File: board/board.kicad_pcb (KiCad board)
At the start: 2 copper layers, 21 x 29 mm, 4 parts, among them J1 009_1000BASE-T, J2 615008145521

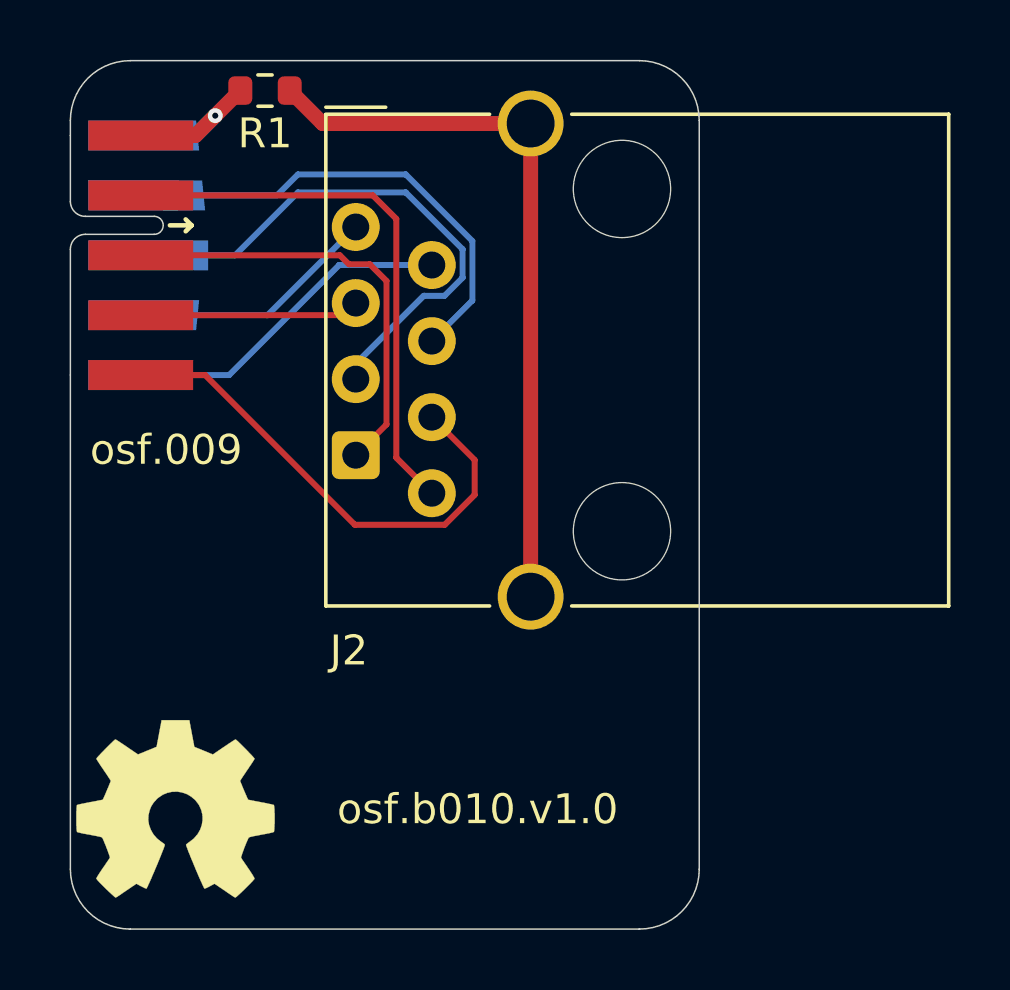
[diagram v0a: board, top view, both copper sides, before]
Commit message: moved tracks for better EMC
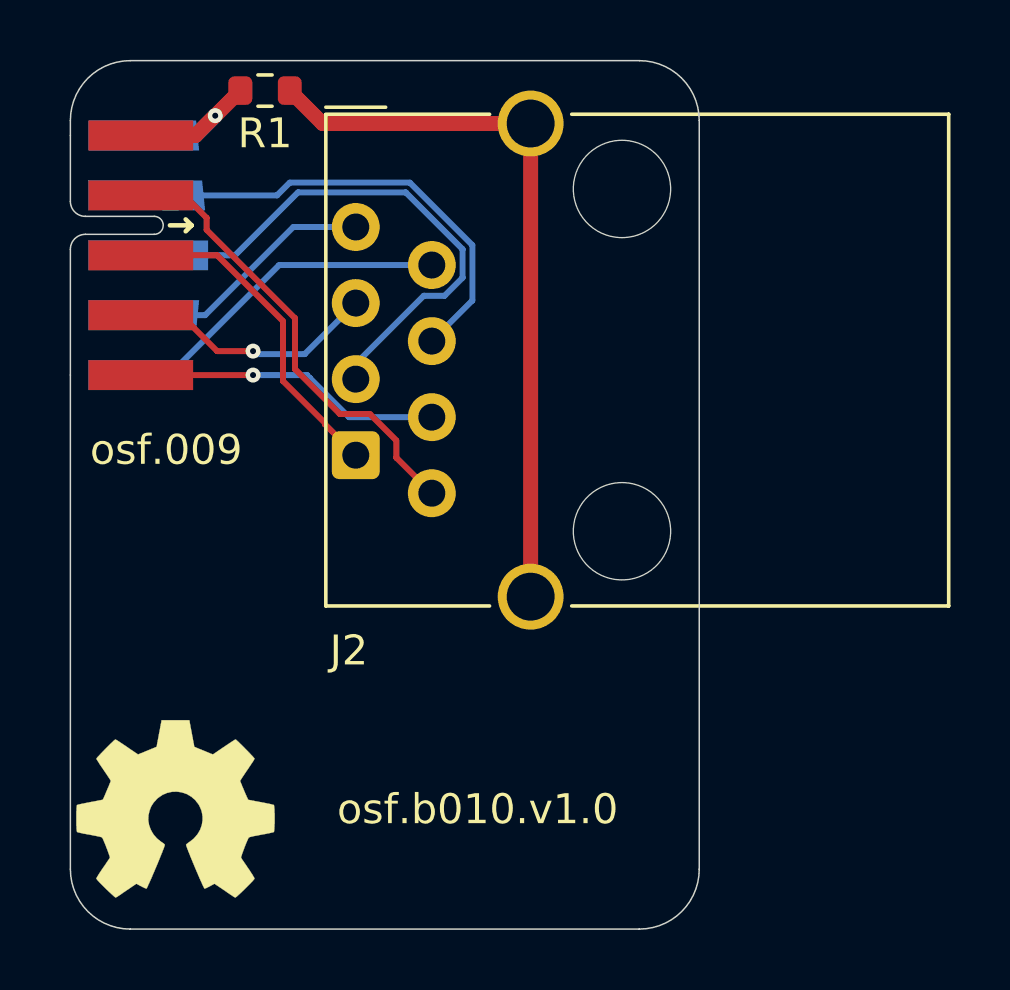
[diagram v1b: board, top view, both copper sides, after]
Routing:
- net /rj45/TD2-: track 16.8 -> 10.3 mm, vias 0 -> 1
- net /rj45/TD1-: track 14.8 -> 11.1 mm
- net /rj45/TD1+: track 18.5 -> 15.4 mm
- net /rj45/TD2+: track 7.35 -> 8.42 mm, vias 0 -> 1
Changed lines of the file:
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@@
   (segment (start 142.4 92.5) (end 144.175 92.5) (width 0.5) (layer "B.Cu") (net 1))
   (segment (start 144.175 92.5) (end 144.8375 91.8375) (width 0.5) (layer "B.Cu") (net 1))
+  (segment (start 147.5 98.6) (end 144.55 95.65) (width 0.2) (layer "F.Cu") (net 2))
+  (segment (start 150 101.8) (end 149 101.8) (width 0.2) (layer "F.Cu") (net 2))
+  (segment (start 144.55 95.25) (end 143.8 94.5) (width 0.2) (layer "F.Cu") (net 2))
   (segment (start 152.07 104.445) (end 150.884 103.259) (width 0.2) (layer "F.Cu") (net 2))
-  (segment (start 150.884 95.284) (end 150.1 94.5) (width 0.2) (layer "F.Cu") (net 2))
-  (segment (start 150.884 103.259) (end 150.884 95.284) (width 0.2) (layer "F.Cu") (net 2))
-  (segment (start 150.1 94.5) (end 142.35 94.5) (width 0.2) (layer "F.Cu") (net 2))
-  (segment (start 150.557 102.148) (end 149.53 103.175) (width 0.2) (layer "F.Cu") (net 3))
-  (segment (start 149.3 96.8) (end 150 96.8) (width 0.2) (layer "F.Cu") (net 3))
-  (segment (start 150 96.8) (end 150.557 97.357) (width 0.2) (layer "F.Cu") (net 3))
-  (segment (start 150.557 97.357) (end 150.557 102.148) (width 0.2) (layer "F.Cu") (net 3))
-  (segment (start 142.35 96.5) (end 149 96.5) (width 0.2) (layer "F.Cu") (net 3))
-  (segment (start 149 96.5) (end 149.3 96.8) (width 0.2) (layer "F.Cu") (net 3))
-  (segment (start 142.35 98.5) (end 149.125 98.5) (width 0.2) (layer "F.Cu") (net 4))
-  (segment (start 149.125 98.5) (end 149.53 98.095) (width 0.2) (layer "F.Cu") (net 4))
-  (segment (start 149.5 105.5) (end 152.5 105.5) (width 0.2) (layer "F.Cu") (net 5))
-  (segment (start 152.5 105.5) (end 153.5 104.5) (width 0.2) (layer "F.Cu") (net 5))
-  (segment (start 153.5 103.335) (end 152.07 101.905) (width 0.2) (layer "F.Cu") (net 5))
-  (segment (start 142.35 100.5) (end 144.5 100.5) (width 0.2) (layer "F.Cu") (net 5))
-  (segment (start 153.5 104.5) (end 153.5 103.335) (width 0.2) (layer "F.Cu") (net 5))
-  (segment (start 144.5 100.5) (end 149.5 105.5) (width 0.2) (layer "F.Cu") (net 5))
-  (segment (start 151.2 93.8) (end 153.424 96.024) (width 0.2) (layer "B.Cu") (net 6))
+  (segment (start 149 101.8) (end 147.5 100.3) (width 0.2) (layer "F.Cu") (net 2))
+  (segment (start 147.5 100.3) (end 147.5 98.6) (width 0.2) (layer "F.Cu") (net 2))
+  (segment (start 143.8 94.5) (end 142.35 94.5) (width 0.2) (layer "F.Cu") (net 2))
+  (segment (start 150.884 102.684) (end 150 101.8) (width 0.2) (layer "F.Cu") (net 2))
+  (segment (start 144.55 95.65) (end 144.55 95.25) (width 0.2) (layer "F.Cu") (net 2))
+  (segment (start 150.884 103.259) (end 150.884 102.684) (width 0.2) (layer "F.Cu") (net 2))
+  (segment (start 144.9 96.5) (end 142.35 96.5) (width 0.2) (layer "F.Cu") (net 3))
+  (segment (start 148.503 102.148) (end 148.503 102.103) (width 0.2) (layer "F.Cu") (net 3))
+  (segment (start 148.503 102.103) (end 147.1 100.7) (width 0.2) (layer "F.Cu") (net 3))
+  (segment (start 147.1 100.7) (end 147.1 98.7) (width 0.2) (layer "F.Cu") (net 3))
+  (segment (start 147.1 98.7) (end 144.9 96.5) (width 0.2) (layer "F.Cu") (net 3))
+  (segment (start 149.53 103.175) (end 148.503 102.148) (width 0.2) (layer "F.Cu") (net 3))
+  (segment (start 146.1 99.7) (end 144.9 99.7) (width 0.2) (layer "F.Cu") (net 4))
+  (segment (start 144.9 99.7) (end 143.7 98.5) (width 0.2) (layer "F.Cu") (net 4))
+  (segment (start 143.7 98.5) (end 142.35 98.5) (width 0.2) (layer "F.Cu") (net 4))
+  (via (at 146.1 99.7) (size 0.5) (drill 0.2) (layers "F.Cu" "B.Cu") (net 4))
+  (segment (start 147.825 99.8) (end 147.5 99.8) (width 0.2) (layer "B.Cu") (net 4))
+  (segment (start 146.2 99.8) (end 146.1 99.7) (width 0.2) (layer "B.Cu") (net 4))
+  (segment (start 147.5 99.8) (end 146.2 99.8) (width 0.2) (layer "B.Cu") (net 4))
+  (segment (start 149.53 98.095) (end 147.825 99.8) (width 0.2) (layer "B.Cu") (net 4))
+  (segment (start 146.1 100.5) (end 142.35 100.5) (width 0.2) (layer "F.Cu") (net 5))
+  (via (at 146.1 100.5) (size 0.5) (drill 0.2) (layers "F.Cu" "B.Cu") (net 5))
+  (segment (start 149.305 101.905) (end 148 100.6) (width 0.2) (layer "B.Cu") (net 5))
+  (segment (start 148 100.6) (end 147.9 100.5) (width 0.2) (layer "B.Cu") (net 5))
+  (segment (start 147.9 100.5) (end 146.1 100.5) (width 0.2) (layer "B.Cu") (net 5))
+  (segment (start 152.07 101.905) (end 149.305 101.905) (width 0.2) (layer "B.Cu") (net 5))
+  (segment (start 147.327 94.073) (end 151.335448 94.073) (width 0.2) (layer "B.Cu") (net 6))
+  (segment (start 142.1 94.5) (end 146.9 94.5) (width 0.2) (layer "B.Cu") (net 6))
   (segment (start 153.424 98.011) (end 152.07 99.365) (width 0.2) (layer "B.Cu") (net 6))
-  (segment (start 147.6 93.8) (end 151.2 93.8) (width 0.2) (layer "B.Cu") (net 6))
-  (segment (start 142.1 94.5) (end 146.9 94.5) (width 0.2) (layer "B.Cu") (net 6))
-  (segment (start 153.424 96.024) (end 153.424 98.011) (width 0.2) (layer "B.Cu") (net 6))
-  (segment (start 146.9 94.5) (end 147.6 93.8) (width 0.2) (layer "B.Cu") (net 6))
+  (segment (start 146.9 94.5) (end 147.327 94.073) (width 0.2) (layer "B.Cu") (net 6))
+  (segment (start 153.424 96.161552) (end 153.424 98.011) (width 0.2) (layer "B.Cu") (net 6))
+  (segment (start 151.335448 94.073) (end 153.424 96.161552) (width 0.2) (layer "B.Cu") (net 6))
   (segment (start 151.2 94.4) (end 147.6 94.4) (width 0.2) (layer "B.Cu") (net 7))
   (segment (start 149.53 100.122) (end 151.8 97.852) (width 0.2) (layer "B.Cu") (net 7))
@@
   (segment (start 153.097 97.250398) (end 153.097 96.297) (width 0.2) (layer "B.Cu") (net 7))
   (segment (start 145.5 96.5) (end 142.6 96.5) (width 0.2) (layer "B.Cu") (net 7))
-  (segment (start 142.4 98.5) (end 146.585 98.5) (width 0.2) (layer "B.Cu") (net 8))
-  (segment (start 146.585 98.5) (end 149.53 95.555) (width 0.2) (layer "B.Cu") (net 8))
-  (segment (start 145.3 100.5) (end 148.975 96.825) (width 0.2) (layer "B.Cu") (net 9))
-  (segment (start 148.975 96.825) (end 152.07 96.825) (width 0.2) (layer "B.Cu") (net 9))
-  (segment (start 142.3 100.5) (end 145.3 100.5) (width 0.2) (layer "B.Cu") (net 9))
+  (segment (start 144.5 98.5) (end 147.445 95.555) (width 0.2) (layer "B.Cu") (net 8))
+  (segment (start 142.4 98.5) (end 144.5 98.5) (width 0.2) (layer "B.Cu") (net 8))
+  (segment (start 147.445 95.555) (end 149.53 95.555) (width 0.2) (layer "B.Cu") (net 8))
+  (segment (start 146.975 96.825) (end 152.07 96.825) (width 0.2) (layer "B.Cu") (net 9))
+  (segment (start 143.3 100.5) (end 146.975 96.825) (width 0.2) (layer "B.Cu") (net 9))
+  (segment (start 142.3 100.5) (end 143.3 100.5) (width 0.2) (layer "B.Cu") (net 9))
   (segment (start 155.37 107.9) (end 155.37 92.1) (width 0.5) (layer "F.Cu") (net 10))
   (segment (start 155.37 92.1) (end 148.425 92.1) (width 0.5) (layer "F.Cu") (net 10))
